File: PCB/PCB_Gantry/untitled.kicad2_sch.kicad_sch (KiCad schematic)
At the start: 14 parts

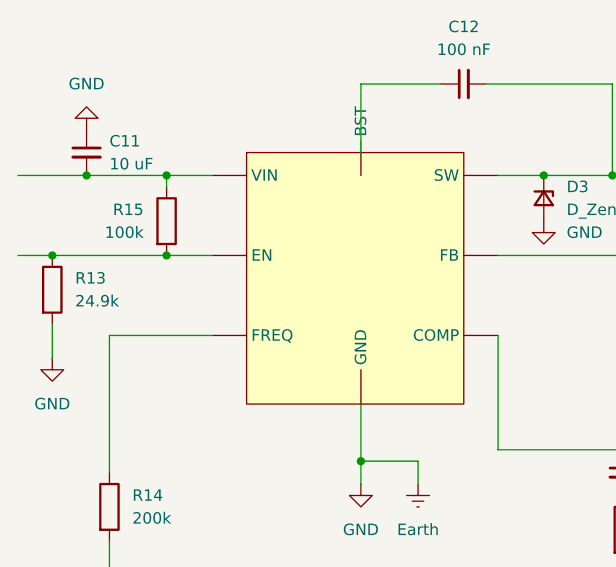
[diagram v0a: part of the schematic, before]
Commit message: Added Schematic
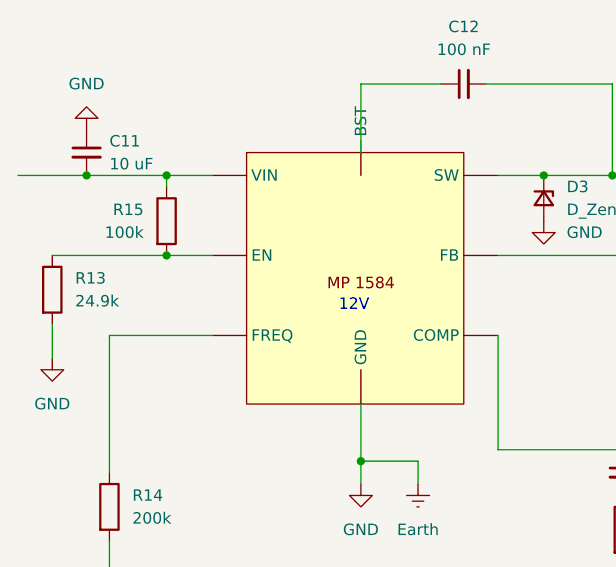
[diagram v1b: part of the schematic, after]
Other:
- note added: "12V"
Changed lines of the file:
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@@
+		)
+	)
+	(text "12V"
+		(exclude_from_sim no)
+		(at 136.398 89.408 0)
+		(effects
+			(font
+				(size 1.27 1.27)
+			)
 		)
 	)
@@
 	)
 	(junction
-		(at 102.87 83.82)
-		(diameter 0)
-		(color 0 0 0 0)
-	)
-	(junction
 		(at 115.57 83.82)
 		(diameter 0)
@@
 	(wire
 		(pts
-			(xy 99.06 83.82) (xy 102.87 83.82)
-		)
-		(stroke
-			(width 0)
-			(type default)
-		)
-	)
-	(wire
-		(pts
 			(xy 177.8 120.65) (xy 166.37 120.65)
 		)
@@
 	)
 	(symbol
+		(lib_id "Components:MP1584")
+		(at 120.65 74.93 0)
+		(unit 1)
+		(exclude_from_sim no)
+		(in_bom yes)
+		(on_board yes)
+		(dnp no)
+		(fields_autoplaced yes)
+		(property "Reference" "U3"
+			(at 136.525 67.31 0)
+			(effects
+				(font
+					(size 1.27 1.27)
+				)
+				(hide yes)
+			)
+		)
+		(property "Value" "~"
+			(at 136.525 69.85 0)
+			(effects
+				(font
+					(size 1.27 1.27)
+				)
+			)
+		)
+		(property "Footprint" ""
+			(at 120.65 74.93 0)
+			(effects
+				(font
+					(size 1.27 1.27)
+				)
+				(hide yes)
+			)
+		)
+		(property "Datasheet" ""
+			(at 120.65 74.93 0)
+			(effects
+				(font
+					(size 1.27 1.27)
+				)
+				(hide yes)
+			)
+		)
+		(property "Description" ""
+			(at 120.65 74.93 0)
+			(effects
+				(font
+					(size 1.27 1.27)
+				)
+				(hide yes)
+			)
+		)
+		(pin ""
+		)
+		(pin ""
+		)
+		(pin ""
+		)
+		(pin ""
+		)
+		(pin ""
+		)
+		(pin ""
+		)
+		(pin ""
+		)
+		(pin ""
+		)
+		(instances
+			(project "PCB_Gantry"
+				(path "/018e7a75-50fa-45c9-b89e-77e71ddfff07/615a1306-801a-41bf-8a6c-987b897a3bec"
+					(reference "U3")
+					(unit 1)
+				)
+			)
+		)
+	)
+	(symbol
 		(lib_id "Device:C_Small")
 		(at 190.5 72.39 0)
@@
 					(unit 1)
 				)
-			)
-		)
-	)
-	(symbol
-		(lib_id "Components:MP1584")
-		(at 120.65 74.93 0)
-		(unit 1)
-		(exclude_from_sim no)
-		(in_bom yes)
-		(on_board yes)
-		(dnp no)
-		(fields_autoplaced yes)
-		(property "Reference" "U3"
-			(at 136.525 67.31 0)
-			(effects
-				(font
-					(size 1.27 1.27)
-				)
-				(hide yes)
-			)
-		)
-		(property "Value" "~"
-			(at 136.525 69.85 0)
-			(effects
-				(font
-					(size 1.27 1.27)
-				)
-			)
-		)
-		(property "Footprint" ""
-			(at 120.65 74.93 0)
-			(effects
-				(font
-					(size 1.27 1.27)
-				)
-				(hide yes)
-			)
-		)
-		(property "Datasheet" ""
-			(at 120.65 74.93 0)
-			(effects
-				(font
-					(size 1.27 1.27)
-				)
-				(hide yes)
-			)
-		)
-		(property "Description" ""
-			(at 120.65 74.93 0)
-			(effects
-				(font
-					(size 1.27 1.27)
-				)
-				(hide yes)
-			)
-		)
-		(pin ""
-		)
-		(pin ""
-		)
-		(pin ""
-		)
-		(pin ""
-		)
-		(pin ""
-		)
-		(pin ""
-		)
-		(pin ""
-		)
-		(pin ""
-		)
-		(instances
-			(project "PCB_Gantry"
-				(path "/018e7a75-50fa-45c9-b89e-77e71ddfff07/615a1306-801a-41bf-8a6c-987b897a3bec"
-					(reference "U3")
-					(unit 1)
-				)
